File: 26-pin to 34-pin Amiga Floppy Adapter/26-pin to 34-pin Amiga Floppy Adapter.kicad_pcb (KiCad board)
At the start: 2 copper layers, 71.1 x 39.4 mm, 75 parts, among them CN1 Conn_02x13_Odd_Even, CN2 Conn_02x17_Odd_Even, CN3 Conn_01x04

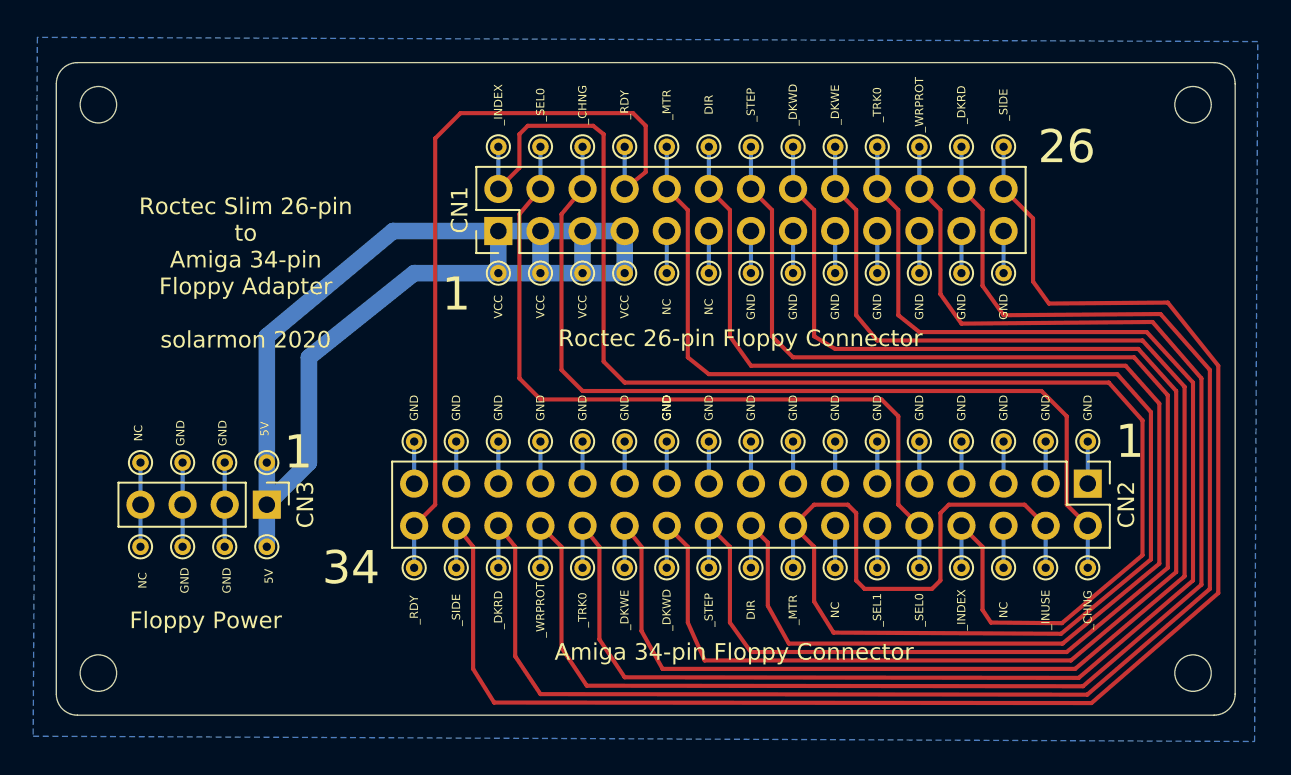
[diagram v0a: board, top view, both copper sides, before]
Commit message: Tweaked dimensions
Tweaked dimensions to 70mmx40mm
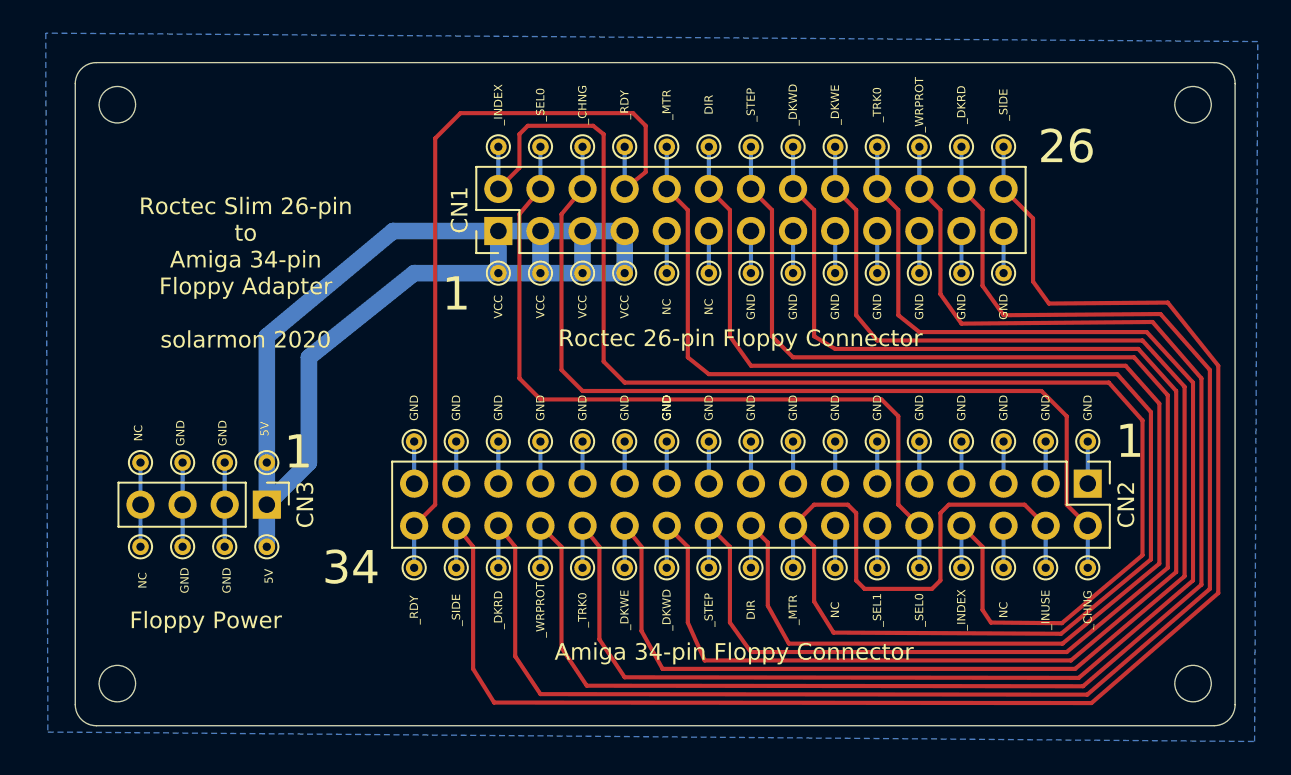
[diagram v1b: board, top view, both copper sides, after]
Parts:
- moved ? 1.31 mm to (93.9, 122.6)
- moved ? 1.14 mm to (93.9, 87.6)
- moved ? 0.64 mm to (158.8, 122.6)
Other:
- board size 71.1 x 39.4 mm -> 70 x 40 mm
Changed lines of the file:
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@@
   )
   (module MountingHole:MountingHole_2.2mm_M2 (layer F.Cu)
-    (at 92.71 87.63)
+    (at 93.853 87.63)
     (descr "Mounting Hole 2.2mm, no annular, M2")
     (tags "mounting hole 2.2mm no annular m2")
@@
   )
   (module MountingHole:MountingHole_2.2mm_M2 (layer F.Cu)
-    (at 92.71 121.92)
+    (at 93.853 122.555)
     (descr "Mounting Hole 2.2mm, no annular, M2")
     (tags "mounting hole 2.2mm no annular m2")
@@
   )
   (module MountingHole:MountingHole_2.2mm_M2 (layer F.Cu)
-    (at 158.75 121.92)
+    (at 158.75 122.555)
     (descr "Mounting Hole 2.2mm, no annular, M2")
     (tags "mounting hole 2.2mm no annular m2")
@@
     (effects (font (size 1 1) (thickness 0.125)) (justify mirror))
   )
-  (gr_arc (start 91.44 123.19) (end 90.17 123.19) (angle -90) (layer Edge.Cuts) (width 0.05))
-  (gr_arc (start 160.02 123.19) (end 160.02 124.46) (angle -90) (layer Edge.Cuts) (width 0.05))
+  (gr_arc (start 92.583 123.825) (end 91.313 123.825) (angle -90) (layer Edge.Cuts) (width 0.05))
+  (gr_arc (start 160.02 123.825) (end 160.02 125.095) (angle -90) (layer Edge.Cuts) (width 0.05))
   (gr_arc (start 160.02 86.36) (end 161.29 86.36) (angle -90) (layer Edge.Cuts) (width 0.05))
-  (gr_arc (start 91.44 86.36) (end 91.44 85.09) (angle -90) (layer Edge.Cuts) (width 0.05))
-  (gr_line (start 90.17 123.19) (end 90.17 86.36) (layer Edge.Cuts) (width 0.05))
-  (gr_line (start 160.02 124.46) (end 91.44 124.46) (layer Edge.Cuts) (width 0.05))
-  (gr_line (start 161.29 86.36) (end 161.29 123.19) (layer Edge.Cuts) (width 0.05))
-  (gr_line (start 91.44 85.09) (end 160.02 85.09) (layer Edge.Cuts) (width 0.05))
+  (gr_arc (start 92.583 86.36) (end 92.583 85.09) (angle -90) (layer Edge.Cuts) (width 0.05))
+  (gr_line (start 91.313 123.825) (end 91.313 86.36) (layer Edge.Cuts) (width 0.05))
+  (gr_line (start 160.02 125.095) (end 92.583 125.095) (layer Edge.Cuts) (width 0.05))
+  (gr_line (start 161.29 86.36) (end 161.29 123.825) (layer Edge.Cuts) (width 0.05))
+  (gr_line (start 92.583 85.09) (end 160.02 85.09) (layer Edge.Cuts) (width 0.05))
   (gr_text 1 (at 114.3 99.06) (layer B.SilkS)
     (effects (font (size 2 2) (thickness 0.125)) (justify mirror))
@@
     (polygon
       (pts
-        (xy 89.027 83.566) (xy 88.773 125.73) (xy 162.46475 126.0475) (xy 162.65525 83.82)
+        (xy 89.535 83.312) (xy 89.662 125.476) (xy 162.46475 126.0475) (xy 162.65525 83.82)
       )
     )
